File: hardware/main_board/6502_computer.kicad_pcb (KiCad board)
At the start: 2 copper layers, 225.1 x 142 mm, 78 parts, among them J1 Conn_02x20_Odd_Even, J2 Conn_01x40_Socket, J3 Conn_01x40_Socket, J4 Conn_01x02_Pin, J5 RCJ-045, J6 DE9_Pins, J7 Mini-DIN-6, J8 Conn_01x12_Pin, Q1 2SC1815, SW1 SW_Push, U1 6502, U10 74HC138, U11 74HC595, U12 74HC138, U13 6522, U14 74HCT04, U15 MAX232, U16 6551, U17 74HC595, U18 74HC14, U2 74LS574, U3 74LS574, U4 HM62256BLP, U5 74LS574, U6 tms9918, U7 HM62256BLP, U8 74HC00, U9 28C256, Y1 CXO_DIP8, Y2 10.738635Mhz, Y3 1.8432MHz

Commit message: Adds stuff
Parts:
- J6: footprint Connector_Dsub:DSUB-9_Pins_Horizontal_P2.77x2.84mm_EdgePinOffset7.70mm_Housed_MountingHolesOffset9.12mm -> Connector_Dsub:DSUB-9_Socket_Horizontal_P2.77x2.84mm_EdgePinOffset7.70mm_Housed_MountingHolesOffset9.12mm
- moved J6 11.8 mm to (121.3, 149.4)
- moved H2 0.55 mm to (256.9, 23.6)
- moved H4 0.55 mm to (256.9, 154.3)
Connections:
- J5 pad 1: /video/VID -> GND
- J5 pad 2: GND -> /video/VID
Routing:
- net /TxD: track 28.5 -> 37.1 mm
- net /RTS: track 32.7 -> 36.6 mm
- net /video/VID: track 24.1 -> 22.2 mm
- net GND: track 129.5 -> 130.4 mm
- removed copper zone on B.Cu, net GND
- removed copper zone on F.Cu, net GND
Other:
- board text added: "74hc00"
- board text added: "CB2"
- board text removed: "74hc04"

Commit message: updated readme
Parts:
- R1, R2, R3, R4, R5, R6, R7, R8: footprint Resistor_THT:R_Axial_DIN0207_L6.3mm_D2.5mm_P7.62mm_Horizontal -> Resistor_THT:R_Axial_DIN0207_L6.3mm_D2.5mm_P10.16mm_Horizontal
- moved R3 5.46 mm to (97.8, 25.4)
- moved kicad_logo 4.93 mm to (60.7, 19.4)
- moved R2 4.61 mm to (97.8, 28.9)
- moved H3 4.23 mm to (43.5, 150.1)
- moved H4 4.23 mm to (256.8, 150.1)
- moved H1 4.23 mm to (43.5, 19.4)
- moved H2 4.23 mm to (256.8, 19.4)
- moved R7 3.63 mm to (99.6, 144.2)
- moved R8 2.77 mm to (132.8, 143.9)
- moved R5 1.70 mm to (71.5, 155.5)
- moved R4 1.65 mm to (71.5, 151.2)
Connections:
- J1 pad 2: GND -> unconnected-(J1-Pin_2-Pad2)
- J1 pad 31: GND -> unconnected-(J1-Pin_31-Pad31)
- J2 pad 2: GND -> unconnected-(J2-Pin_2-Pad2)
- J2 pad 37: GND -> unconnected-(J2-Pin_37-Pad37)
- J2 pad 38: GND -> unconnected-(J2-Pin_38-Pad38)
- J3 pad 2: GND -> unconnected-(J3-Pin_2-Pad2)
- J3 pad 37: GND -> unconnected-(J3-Pin_37-Pad37)
- J3 pad 38: GND -> unconnected-(J3-Pin_38-Pad38)
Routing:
- net VDD: track 992.2 -> 987.0 mm
- net Net-(D4-A): track 15.8 -> 18.8 mm
- net /video/vram_a0: track 60.7 -> 58.4 mm
- net /video/vram_a1: track 59.2 -> 56.9 mm
- net /video/vram_a2: track 57.8 -> 55.5 mm
- net /video/VID: track 22.2 -> 24.3 mm
- net /video/vram_a3: track 56.2 -> 54.1 mm
- net IRQB: track 499.8 -> 501.8 mm
- net /video/vram_a4: track 54.5 -> 52.7 mm
- net /video/vram_a5: track 53.0 -> 51.3 mm
- net /video/vram_a6: track 51.4 -> 49.8 mm
- net RDY: track 209.7 -> 208.6 mm
- net Net-(D3-A): track 3.18 -> 4.27 mm
- net COMVID: track 71.6 -> 72.4 mm
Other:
- board size 225.1 x 142 mm -> 225.1 x 136.3 mm
- board text added: "v1.1.0"
- board text removed: "v1.0.0"

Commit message: replace load with rx
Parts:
- added H5: MountingHole_Pad, MountingHole:MountingHole_3.2mm_M3_ISO7380_Pad, F.Cu at (207.6, 57.1)
- added H6: MountingHole_Pad, MountingHole:MountingHole_3.2mm_M3_ISO7380_Pad, F.Cu at (207.6, 187.8)
- moved C27 87.7 mm to (148.3, 215.4)
- moved D3 87.7 mm to (138.8, 211.5)
- moved R6 87.7 mm to (152.7, 215.4)
- moved R7 87.7 mm to (155.8, 211.5)
- moved SW1 87.7 mm to (143.7, 215.4)
- moved J6 84.5 mm to (179.8, 210.3)
- moved J5 82.6 mm to (111.4, 219.2)
- moved Q1 82.6 mm to (121.4, 206.1)
- moved R4 82.6 mm to (128.1, 211.3)
- moved J4 82.6 mm to (133.9, 211.3)
- moved R5 82.6 mm to (128.2, 215.6)
- moved J7 81.9 mm to (202.3, 215.6)
- moved J8 80.6 mm to (270.0, 209.6)
- moved REF** 68.7 mm to (143.4, 117.8)
- moved U1 68.7 mm to (169.4, 65.6)
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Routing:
- net VDD: track 987.0 -> 957.9 mm
- net /RTS: track 36.6 -> 10.8 mm
- net /KB_CLK: track 24.8 -> 7.73 mm
- net /TxD: track 37.1 -> 20.4 mm
- net /KB_DAT: track 78.3 -> 62.8 mm
- net ResB: track 510.6 -> 495.2 mm
- net Net-(D4-K): track 29.7 -> 17.0 mm
- net /RxD: track 28.5 -> 18.1 mm
- net COMVID: track 72.4 -> 68.4 mm

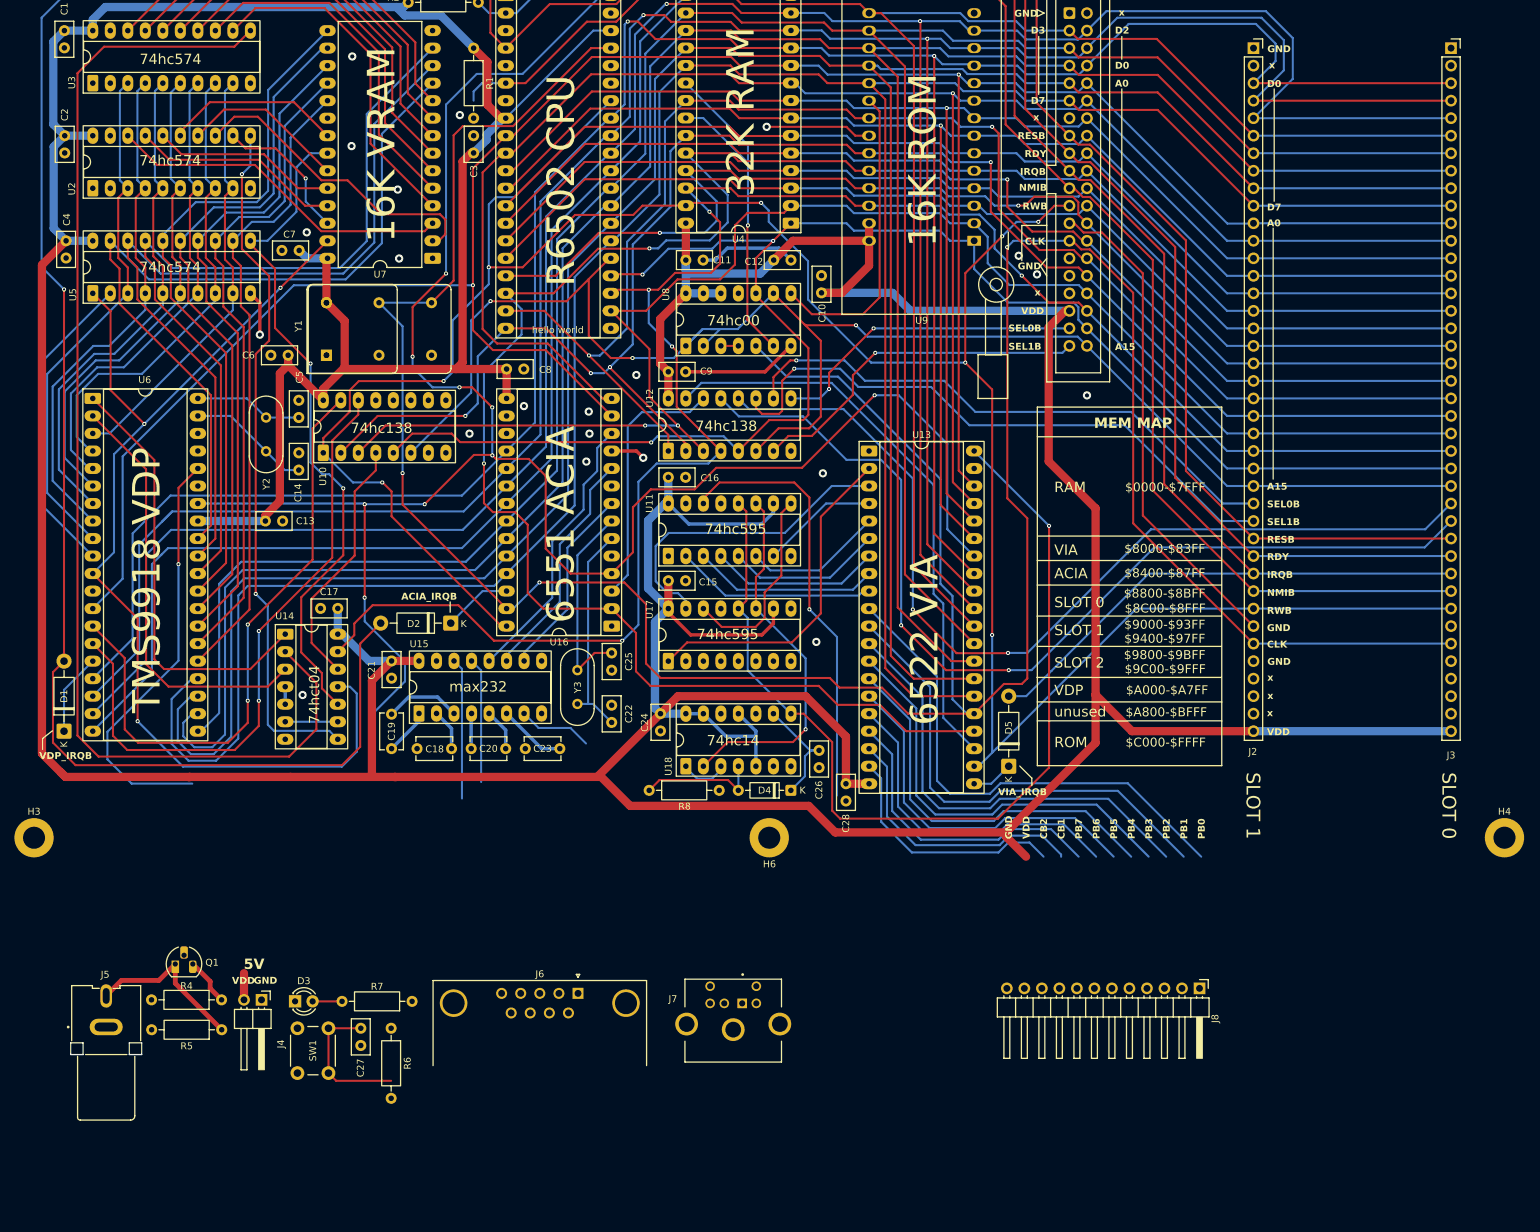
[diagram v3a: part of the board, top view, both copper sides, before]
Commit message: Updated gitignore
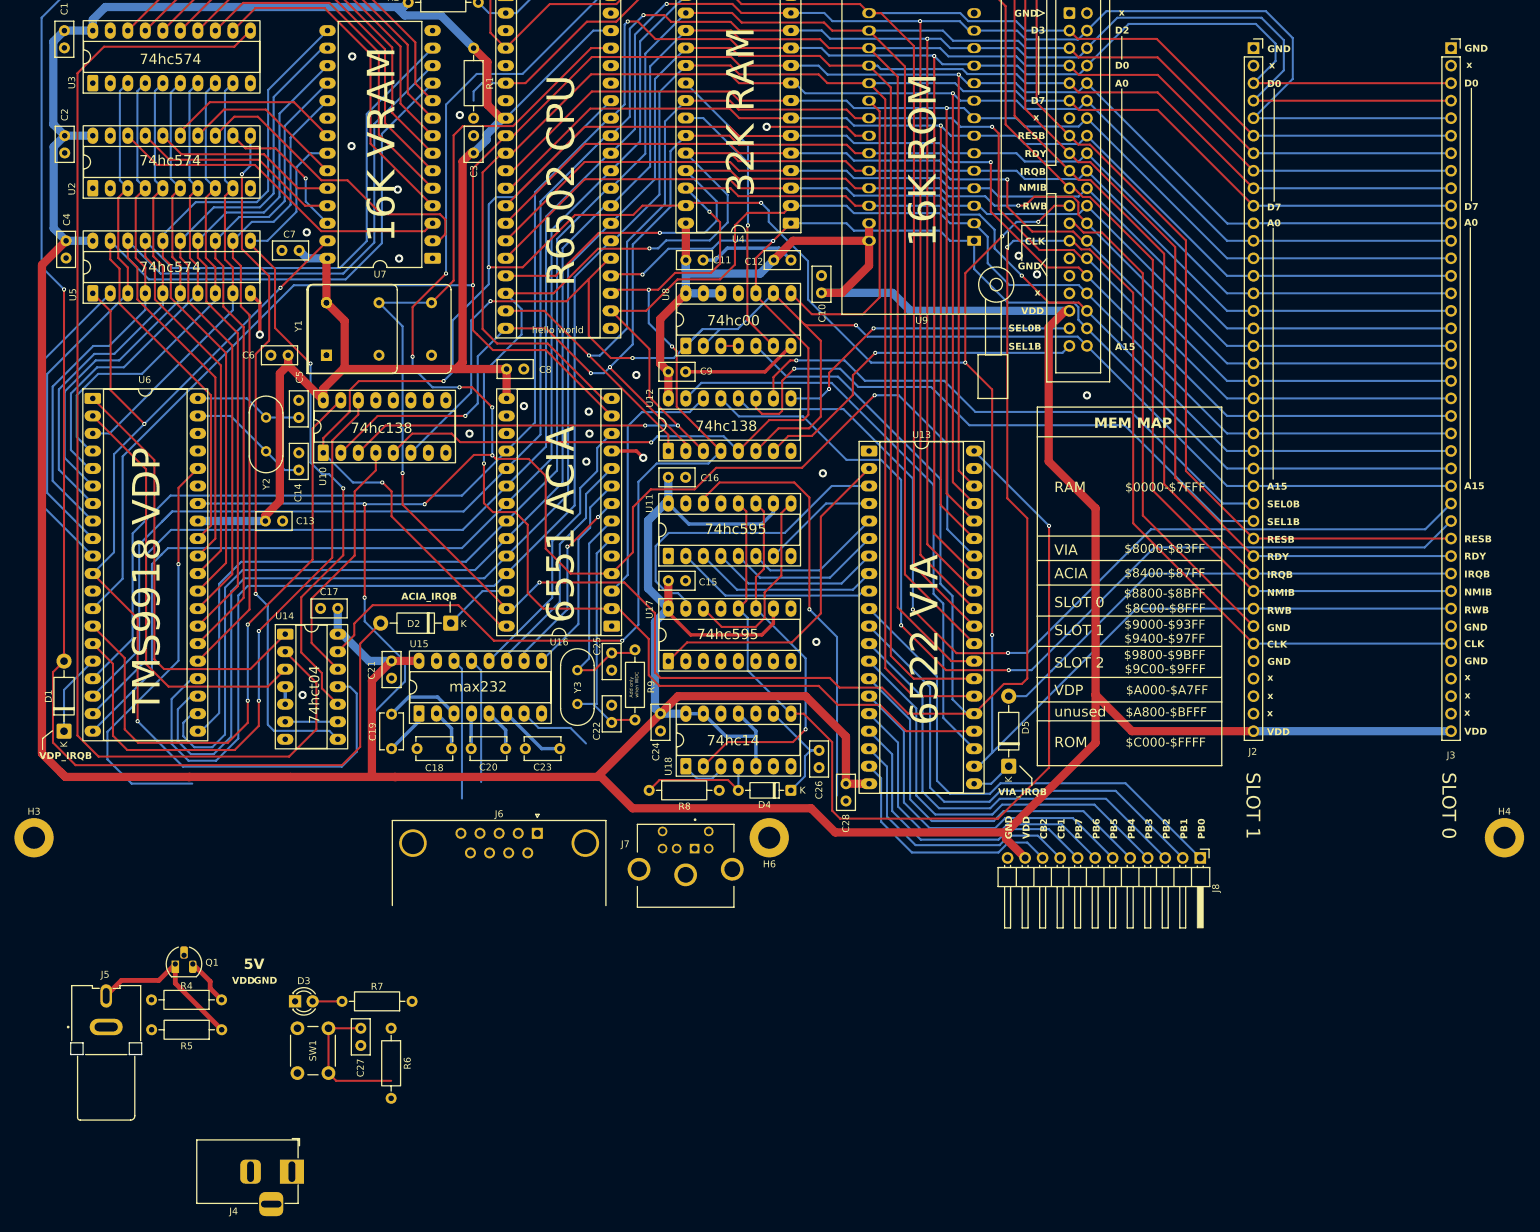
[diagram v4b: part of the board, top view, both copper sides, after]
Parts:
- added R9: 1M, Resistor_THT:R_Axial_DIN0207_L6.3mm_D2.5mm_P10.16mm_Horizontal, F.Cu at (188.1, 170.7)
- C25: value 22pf -> 22/20pf
- J4: value Conn_01x02_Pin -> Barrel_Jack_MountingPin; footprint Connector_PinHeader_2.54mm:PinHeader_1x02_P2.54mm_Horizontal -> Connector_BarrelJack:BarrelJack_Horizontal
- moved J4 25.3 mm to (138.3, 236.2), turned to 0 degrees
- moved J6 23.9 mm to (173.9, 187.1)
- moved J7 23.5 mm to (195.4, 193.2)
- moved J8 18.9 mm to (270.1, 190.7)
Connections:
- U15 pad 9: unconnected-(U15-R2OUT-Pad9) -> /R2OUT
- U16 pad 9: unconnected-(U16-CTSB-Pad9) -> /R2OUT
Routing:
- net /R2OUT: track 0.00 -> 29.6 mm
- net Net-(U16-XTAL1): track 33.0 -> 37.3 mm
- net VDD: track 957.9 -> 954.3 mm
- net Net-(U16-XTAL2): track 29.7 -> 33.3 mm
- net /T2IN: track 28.1 -> 28.4 mm, vias 0 -> 2
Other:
- board text added: "Add only when WDC"
